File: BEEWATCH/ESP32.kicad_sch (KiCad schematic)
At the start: 35 parts, among them U4 W25Q128JVS

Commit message: Components selections
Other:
- note added: "Optional"
- moved on the sheet: C?, R?, U4, Y?

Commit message: Save Kicad files
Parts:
- renumbered U4 to U3

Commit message: Insufficient GPIOs planning to add/C MUX or MCU
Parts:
- added C?: 100nF, symbol Device:C_Small
- added R?: 5K1, symbol Device:R_Small
- R? (x2): value R_Small -> 470
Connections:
- net +3.3V: now also R?.2
- net GND: now also C?.2
- net SPI_CLK: no longer U?.12 (MTCK)
- net SPI_CS0: no longer U?.16 (GPIO10)
- net SPI_D0: no longer U?.13 (MTDO)
- net SPI_DI: no longer U?.6 (GPIO2)
- net SPI_NHLD: no longer U?.9 (MTMS)
- net SPI_NWP: no longer U?.10 (MTDI)
- net GPIO8: now reaches U?.14 (GPIO8)
- net GPIO9: now reaches U?.15 (PROGRAM/GPIO9)
- net RESET: now reaches U?.7 (CHIP_EN)
- net RESET: now also C?.1, R?.1
- net GPIO3: now reaches U?.8 (GPIO3)
- new net GPIO10: U?.16 (FSPICS0/GPIO10)
- new net GPIO2: U?.6 (FSPIQ/GPIO2)
- new net GPIO4: U?.9 (FSPIHD/GPIO4)
- new net GPIO5: U?.10 (FSPIWP/GPIO5)
- new net GPIO6: U?.12 (FSPICLK/GPIO6)
- new net GPIO7: U?.13 (FSPID/GPIO7)
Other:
- note added: "* Optional"
- note added: "* The ESP32 has one I2C channels and any GPIO pin can be set as SDA or SCL. * The SPI2 channels can be set to any GPIO pin"
- note added: "CRYSTALS"
- note added: "ESP32-C3F"
- note added: "EXTERNAL SPI FLASH"
- note added: "USB"
- note removed: "Optional"
- moved on the sheet: ANT1, C?, J?, L?, R?, U3, U?, Y?

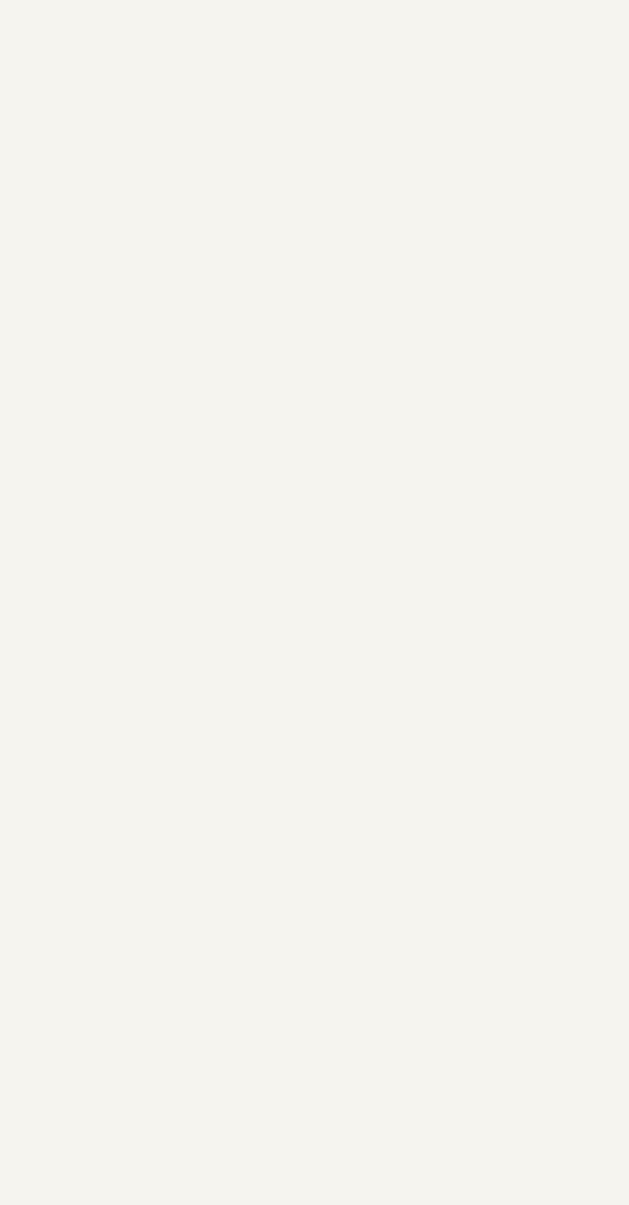
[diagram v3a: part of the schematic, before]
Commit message: planning to shift to ESP32-D0WDQ6
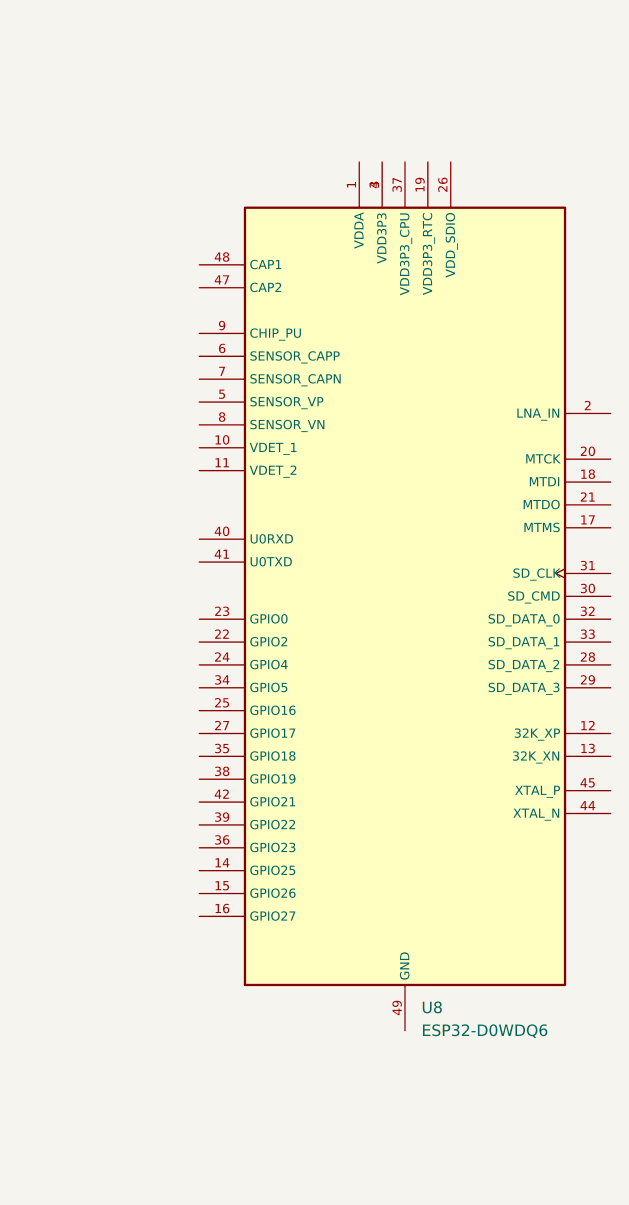
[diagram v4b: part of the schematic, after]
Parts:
- added U8: ESP32-D0WDQ6, Project:VFQFN-48, symbol Project_Library:ESP32-D0WDQ6
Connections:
- new net: U8.3 (VDD3P3), U8.4 (VDD3P3)
- new net VDDA: U8.1 (VDDA), U8.43 (VDDA), U8.46 (VDDA)
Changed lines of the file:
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@@
+    )
+  )
+  (symbol (lib_id "Project_Library:ESP32-D0WDQ6") (at 454.66 98.425 0) (unit 1)
+    (in_bom yes) (on_board yes) (dnp no) (fields_autoplaced)
+    (property "Reference" "U8" (at 456.4889 139.065 0)
+      (effects (font (size 1.27 1.27)) (justify left))
+    )
+    (property "Value" "ESP32-D0WDQ6" (at 456.4889 141.605 0)
+      (effects (font (size 1.27 1.27)) (justify left))
+    )
+    (property "Footprint" "Project:VFQFN-48" (at 438.15 48.895 0)
+      (effects (font (size 1.27 1.27)) hide)
+    )
+    (property "Datasheet" "" (at 438.15 48.895 0)
+      (effects (font (size 1.27 1.27)) hide)
+    )
+    (pin "10")
+    (pin "11")
+    (pin "12")
+    (pin "13")
+    (pin "14")
+    (pin "15")
+    (pin "16")
+    (pin "17")
+    (pin "18")
+    (pin "19")
+    (pin "2")
+    (pin "20")
+    (pin "21")
+    (pin "22")
+    (pin "23")
+    (pin "24")
+    (pin "25")
+    (pin "26")
+    (pin "27")
+    (pin "28")
+    (pin "29")
+    (pin "30")
+    (pin "31")
+    (pin "32")
+    (pin "33")
+    (pin "34")
+    (pin "35")
+    (pin "36")
+    (pin "37")
+    (pin "38")
+    (pin "39")
+    (pin "4")
+    (pin "40")
+    (pin "41")
+    (pin "42")
+    (pin "44")
+    (pin "45")
+    (pin "47")
+    (pin "48")
+    (pin "49")
+    (pin "5")
+    (pin "6")
+    (pin "7")
+    (pin "8")
+    (pin "9")
+    (pin "1")
+    (pin "3")
+    (pin "43")
+    (pin "46")
+    (instances
+      (project "BEEWATCH"
+        (path "/e9c5fb53-480b-4989-8495-a3341ee99514/56d77f8e-c069-456f-a514-fdde13f048cd"
+          (reference "U8") (unit 1)
+        )
+      )
     )
   )
